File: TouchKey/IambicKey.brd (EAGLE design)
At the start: 59.5 x 22.5 mm, 12 parts, among them Q1 MOSFET-NCHANNELSMD, Q2 MOSFET-NCHANNELSMD, U1 AT42QT1012, U2 AT42QT1012

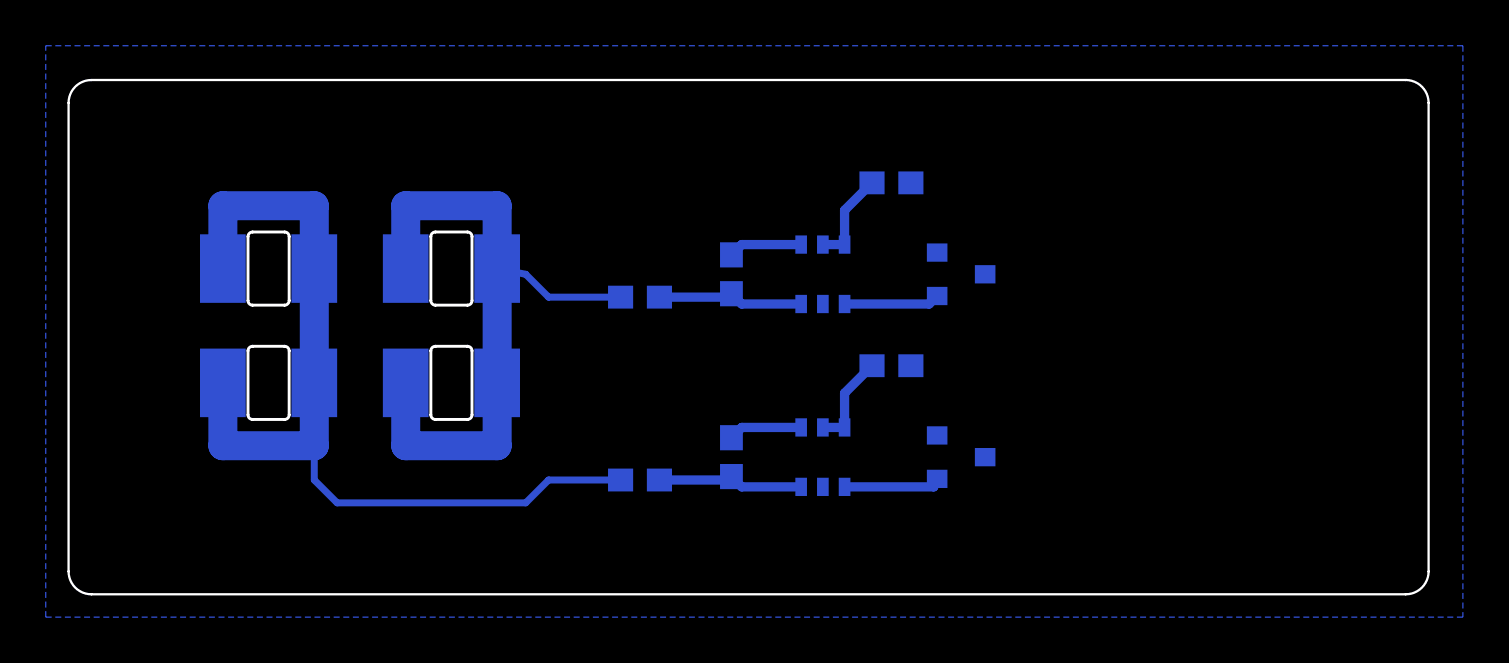
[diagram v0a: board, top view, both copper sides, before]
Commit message: Replaced most through hole components with SMD equivilents
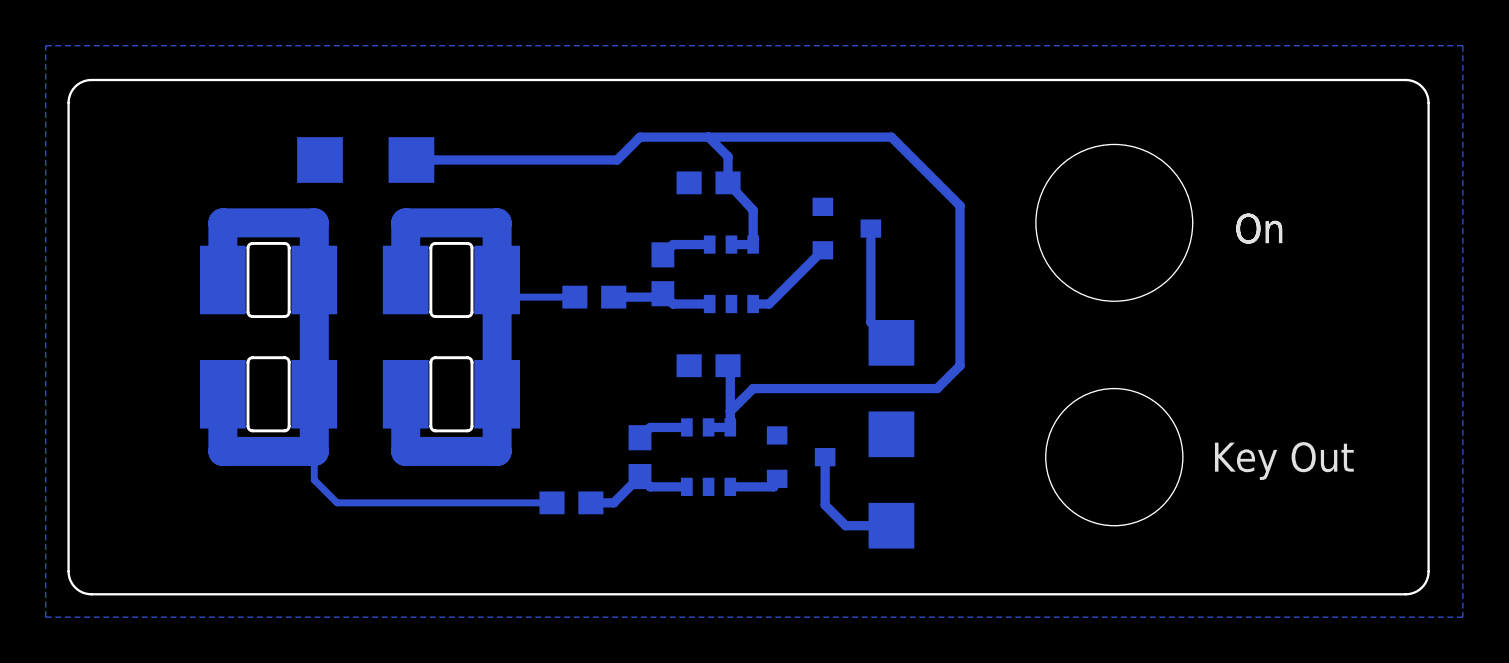
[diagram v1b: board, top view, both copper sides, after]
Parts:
- added TP1, TP2, TP3, TP4, TP5: TPTP20SQ, testpad:TP20SQ
- moved C1 8.00 mm to (30.0, 20.0), turned to 0 degrees
- moved C2 8.00 mm to (30.0, 12.0), turned to 0 degrees
- moved Q1 7.00 mm to (34.0, 8.00)
- moved Q2 5.39 mm to (36.0, 18.0)
- moved U1 5.00 mm to (30.0, 8.00)
- moved C3 4.00 mm to (27.0, 8.00)
- moved U2 4.00 mm to (31.0, 16.0)
- moved R1 3.16 mm to (24.0, 6.00)
- moved C4 3.00 mm to (28.0, 16.0)
- moved R2 2.00 mm to (25.0, 15.0)
- moved U$1 0.50 mm to (10.8, 13.2)
- moved U$2 0.50 mm to (18.8, 13.2)
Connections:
- new net N$10: Q1.3, TP1.TP
- new net N$11: Q2.3, TP2.TP
- net GND: now also TP4.TP, TP5.TP
- net VCC: now also TP3.TP
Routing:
- net VCC: track 8.29 -> 53.6 mm
- net N$11: track 0.00 -> 5.37 mm
- net N$10: track 0.00 -> 5.37 mm
- net N$5: track 39.7 -> 35.1 mm
- net N$8: track 29.8 -> 26.9 mm
- net N$7: track 6.45 -> 4.45 mm
- net N$1: track 4.28 -> 2.28 mm
- net N$4: track 6.45 -> 4.86 mm
- net N$6: track 3.24 -> 2.24 mm
- net N$3: track 3.24 -> 2.24 mm
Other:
- board text added: "AV15152"
- board text added: "Key Out"
- board text added: "On"
